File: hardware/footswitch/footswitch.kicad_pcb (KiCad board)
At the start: 2 copper layers, 34 x 58 mm, 6 parts, among them J1 Conn_02x05_Counter_Clockwise

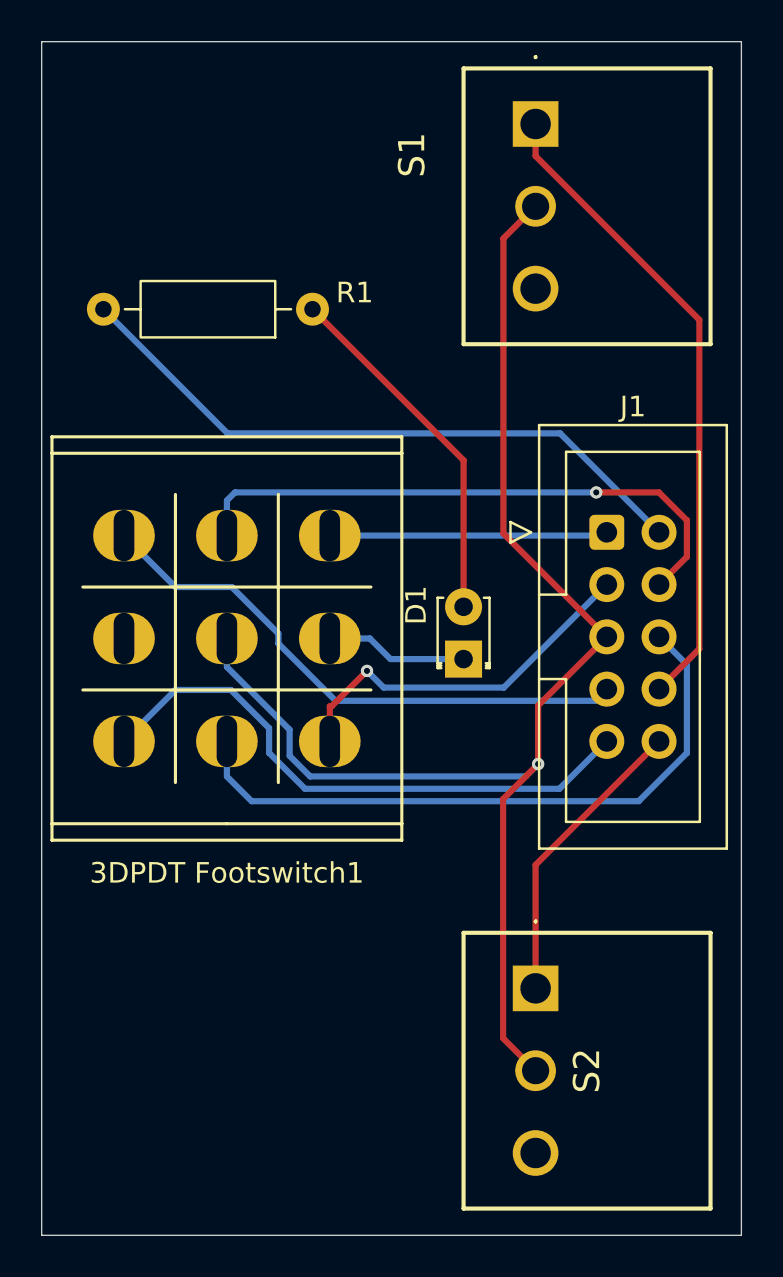
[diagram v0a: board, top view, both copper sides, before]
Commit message: Track adjustments to footswitch board
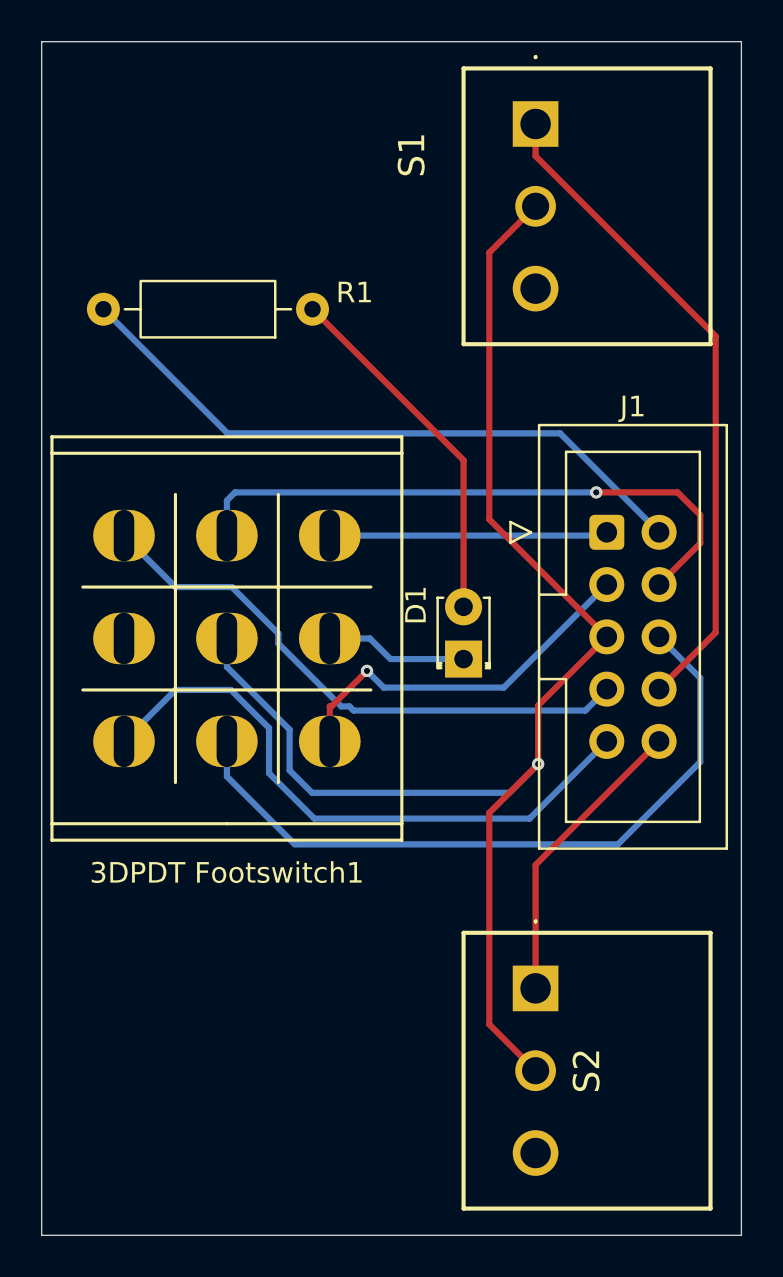
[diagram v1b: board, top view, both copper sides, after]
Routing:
- net /conn6: track 31.7 -> 34.6 mm
- net /conn5: track 67.2 -> 69.4 mm
- net /conn9: track 28.1 -> 29.9 mm
- net /conn4: track 28.5 -> 29.5 mm
- net /conn8: track 31.6 -> 32.2 mm
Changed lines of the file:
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@@
 	)
 	(segment
-		(start 157.46 99)
-		(end 155.1566 101.3034)
-		(width 0.3)
-		(layer "B.Cu")
-		(net 2)
-	)
-	(segment
-		(start 155.1566 101.3034)
-		(end 142.7959 101.3034)
+		(start 143.25 102.75)
+		(end 141.0511 100.5511)
+		(width 0.3)
+		(layer "B.Cu")
+		(net 2)
+	)
+	(segment
+		(start 141.0511 98.3552)
+		(end 139.1959 96.5)
+		(width 0.3)
+		(layer "B.Cu")
+		(net 2)
+	)
+	(segment
+		(start 136.5 96.5)
+		(end 134 99)
 		(width 0.3)
 		(layer "B.Cu")
@@
 	)
 	(segment
-		(start 142.7959 101.3034)
-		(end 141.0511 99.5586)
-		(width 0.3)
-		(layer "B.Cu")
-		(net 2)
-	)
-	(segment
-		(start 141.0511 99.5586)
+		(start 141.0511 100.5511)
 		(end 141.0511 98.3552)
 		(width 0.3)
@@
 	)
 	(segment
-		(start 141.0511 98.3552)
-		(end 139.1959 96.5)
-		(width 0.3)
-		(layer "B.Cu")
-		(net 2)
-	)
-	(segment
-		(start 136.5 96.5)
-		(end 134 99)
-		(width 0.3)
-		(layer "B.Cu")
-		(net 2)
+		(start 157.46 99)
+		(end 153.71 102.75)
+		(width 0.3)
+		(layer "B.Cu")
+		(net 2)
+	)
+	(segment
+		(start 153.71 102.75)
+		(end 143.25 102.75)
+		(width 0.3)
+		(layer "B.Cu")
+		(net 2)
+	)
+	(segment
+		(start 162 89.38)
+		(end 162 88)
+		(width 0.3)
+		(layer "F.Cu")
+		(net 3)
+	)
+	(segment
+		(start 160.9023 86.9023)
+		(end 156.9469 86.9023)
+		(width 0.3)
+		(layer "F.Cu")
+		(net 3)
+	)
+	(segment
+		(start 162 88)
+		(end 160.9023 86.9023)
+		(width 0.3)
+		(layer "F.Cu")
+		(net 3)
 	)
 	(segment
 		(start 160 91.38)
-		(end 161.3519 90.0281)
-		(width 0.3)
-		(layer "F.Cu")
-		(net 3)
-	)
-	(segment
-		(start 159.9971 86.9023)
-		(end 156.9469 86.9023)
-		(width 0.3)
-		(layer "F.Cu")
-		(net 3)
-	)
-	(segment
-		(start 161.3519 88.2571)
-		(end 159.9971 86.9023)
-		(width 0.3)
-		(layer "F.Cu")
-		(net 3)
-	)
-	(segment
-		(start 161.3519 90.0281)
-		(end 161.3519 88.2571)
+		(end 162 89.38)
 		(width 0.3)
 		(layer "F.Cu")
@@
 	)
 	(segment
+		(start 144.5542 97.299)
+		(end 141.5 94.2448)
+		(width 0.3)
+		(layer "B.Cu")
+		(net 5)
+	)
+	(segment
 		(start 141.5 94.2448)
 		(end 141.5 93.7597)
@@
 	)
 	(segment
-		(start 156.8917 97.0283)
-		(end 144.2835 97.0283)
+		(start 141.5 93.7597)
+		(end 139.2403 91.5)
+		(width 0.3)
+		(layer "B.Cu")
+		(net 5)
+	)
+	(segment
+		(start 145.155577 97.5)
+		(end 144.954577 97.299)
 		(width 0.3)
 		(layer "B.Cu")
@@
 	)
 	(segment
+		(start 156.42 97.5)
+		(end 145.155577 97.5)
+		(width 0.3)
+		(layer "B.Cu")
+		(net 5)
+	)
+	(segment
+		(start 144.954577 97.299)
+		(end 144.5542 97.299)
+		(width 0.3)
+		(layer "B.Cu")
+		(net 5)
+	)
+	(segment
 		(start 157.46 96.46)
-		(end 156.8917 97.0283)
+		(end 156.42 97.5)
 		(width 0.3)
 		(layer "B.Cu")
@@
 		(start 136.5 91.5)
 		(end 134 89)
-		(width 0.3)
-		(layer "B.Cu")
-		(net 5)
-	)
-	(segment
-		(start 141.5 93.7597)
-		(end 139.2403 91.5)
-		(width 0.3)
-		(layer "B.Cu")
-		(net 5)
-	)
-	(segment
-		(start 144.2835 97.0283)
-		(end 141.5 94.2448)
 		(width 0.3)
 		(layer "B.Cu")
@@
 	)
 	(segment
-		(start 159.0079 101.9051)
-		(end 161.3508 99.5622)
-		(width 0.3)
-		(layer "B.Cu")
-		(net 7)
-	)
-	(segment
 		(start 139 99)
 		(end 139 100.7017)
@@
 	)
 	(segment
-		(start 161.3508 99.5622)
-		(end 161.3508 95.2708)
-		(width 0.3)
-		(layer "B.Cu")
-		(net 7)
-	)
-	(segment
-		(start 161.3508 95.2708)
+		(start 142.2983 104)
+		(end 158 104)
+		(width 0.3)
+		(layer "B.Cu")
+		(net 7)
+	)
+	(segment
+		(start 139 100.7017)
+		(end 142.2983 104)
+		(width 0.3)
+		(layer "B.Cu")
+		(net 7)
+	)
+	(segment
+		(start 162 95.92)
 		(end 160 93.92)
 		(width 0.3)
@@
 	)
 	(segment
-		(start 139 100.7017)
-		(end 140.2034 101.9051)
-		(width 0.3)
-		(layer "B.Cu")
-		(net 7)
-	)
-	(segment
-		(start 140.2034 101.9051)
-		(end 159.0079 101.9051)
+		(start 158 104)
+		(end 162 100)
+		(width 0.3)
+		(layer "B.Cu")
+		(net 7)
+	)
+	(segment
+		(start 162 100)
+		(end 162 95.92)
 		(width 0.3)
 		(layer "B.Cu")
@@
 	)
 	(segment
-		(start 154 73)
-		(end 152.438 74.562)
-		(width 0.3)
-		(layer "F.Cu")
-		(net 9)
-	)
-	(segment
-		(start 152.4226 113.4226)
-		(end 152.4226 101.8022)
-		(width 0.3)
-		(layer "F.Cu")
-		(net 9)
-	)
-	(segment
 		(start 154.125 97.255)
 		(end 157.46 93.92)
@@
 	)
 	(segment
-		(start 152.438 74.562)
-		(end 152.438 88.898)
-		(width 0.3)
-		(layer "F.Cu")
-		(net 9)
-	)
-	(segment
-		(start 152.438 88.898)
+		(start 151.75 88.21)
 		(end 157.46 93.92)
 		(width 0.3)
@@
 	)
 	(segment
-		(start 152.4226 101.8022)
-		(end 154.125 100.0998)
+		(start 154 115)
+		(end 151.75 112.75)
+		(width 0.3)
+		(layer "F.Cu")
+		(net 9)
+	)
+	(segment
+		(start 151.75 75.25)
+		(end 151.75 88.21)
 		(width 0.3)
 		(layer "F.Cu")
@@
 	)
 	(segment
-		(start 154 115)
-		(end 152.4226 113.4226)
+		(start 151.75 112.75)
+		(end 151.75 102.4748)
+		(width 0.3)
+		(layer "F.Cu")
+		(net 9)
+	)
+	(segment
+		(start 154 73)
+		(end 151.75 75.25)
+		(width 0.3)
+		(layer "F.Cu")
+		(net 9)
+	)
+	(segment
+		(start 151.75 102.4748)
+		(end 154.125 100.0998)
 		(width 0.3)
 		(layer "F.Cu")
@@
 	)
 	(segment
-		(start 143.0451 100.7017)
-		(end 153.5231 100.7017)
-		(width 0.3)
-		(layer "B.Cu")
-		(net 9)
-	)
-	(segment
 		(start 142.0483 98.4309)
-		(end 142.0483 99.7049)
+		(end 142.0483 100.40609)
+		(width 0.3)
+		(layer "B.Cu")
+		(net 9)
+	)
+	(segment
+		(start 142.0483 100.40609)
+		(end 143.14221 101.5)
+		(width 0.3)
+		(layer "B.Cu")
+		(net 9)
+	)
+	(segment
+		(start 143.14221 101.5)
+		(end 152.7248 101.5)
+		(width 0.3)
+		(layer "B.Cu")
+		(net 9)
+	)
+	(segment
+		(start 152.7248 101.5)
+		(end 154.125 100.0998)
 		(width 0.3)
 		(layer "B.Cu")
@@
 	)
 	(segment
-		(start 153.5231 100.7017)
-		(end 154.125 100.0998)
-		(width 0.3)
-		(layer "B.Cu")
-		(net 9)
-	)
-	(segment
 		(start 139 95.3826)
 		(end 142.0483 98.4309)
@@
 	)
 	(segment
-		(start 142.0483 99.7049)
-		(end 143.0451 100.7017)
-		(width 0.3)
-		(layer "B.Cu")
-		(net 9)
+		(start 162.75 93.71)
+		(end 162.75 79.3117)
+		(width 0.3)
+		(layer "F.Cu")
+		(net 10)
+	)
+	(segment
+		(start 162.75 79.3117)
+		(end 154 70.5617)
+		(width 0.3)
+		(layer "F.Cu")
+		(net 10)
+	)
+	(segment
+		(start 154 70.5617)
+		(end 154 69)
+		(width 0.3)
+		(layer "F.Cu")
+		(net 10)
 	)
 	(segment
 		(start 160 96.46)
-		(end 161.9536 94.5064)
-		(width 0.3)
-		(layer "F.Cu")
-		(net 10)
-	)
-	(segment
-		(start 154 69)
-		(end 154 70.5617)
-		(width 0.3)
-		(layer "F.Cu")
-		(net 10)
-	)
-	(segment
-		(start 161.9536 94.5064)
-		(end 161.9536 78.5153)
-		(width 0.3)
-		(layer "F.Cu")
-		(net 10)
-	)
-	(segment
-		(start 161.9536 78.5153)
-		(end 154 70.5617)
-		(width 0.3)
-		(layer "F.Cu")
+		(end 162.75 93.71)
+		(width 0.3)
+		(layer "F.Cu")

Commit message: Adjust footprint for dpdt alpha
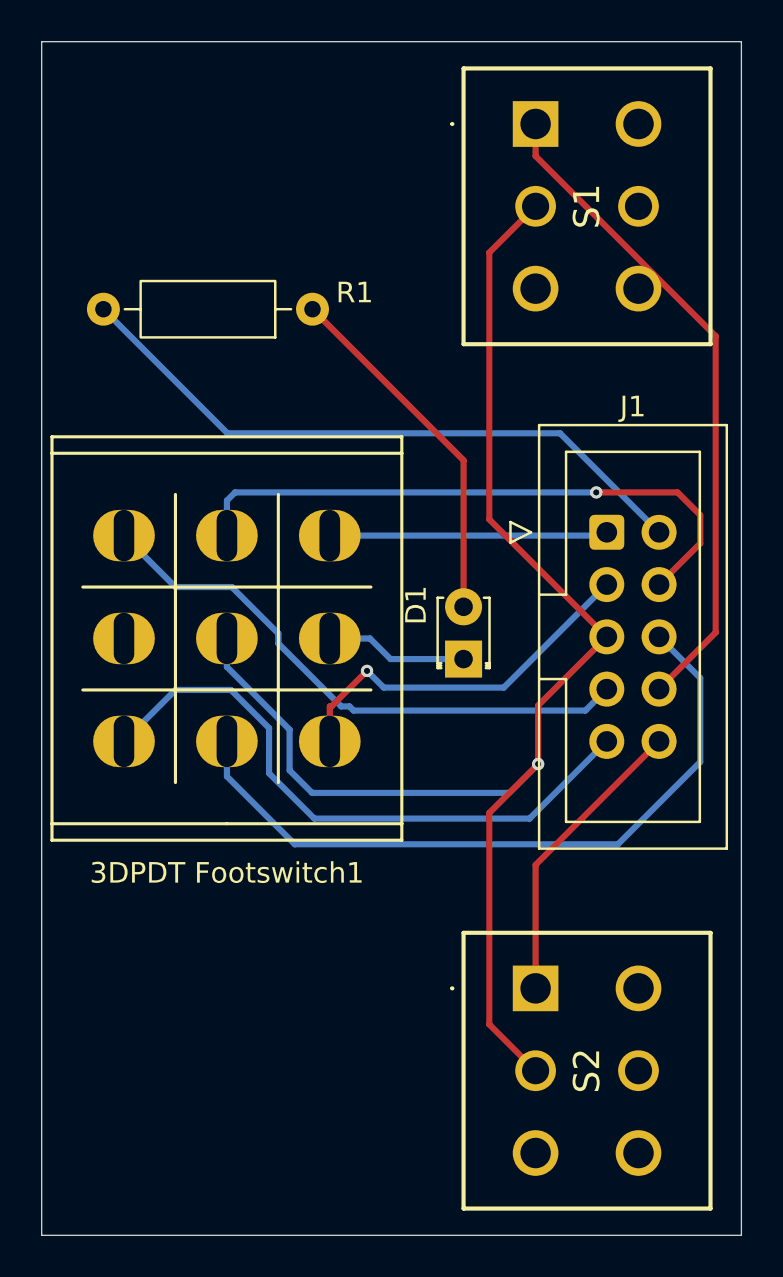
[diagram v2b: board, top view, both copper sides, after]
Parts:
- S1, S2: footprint pcb switch:SF12011F010220RM050 -> pcb switch:DPDT momentary footswitch

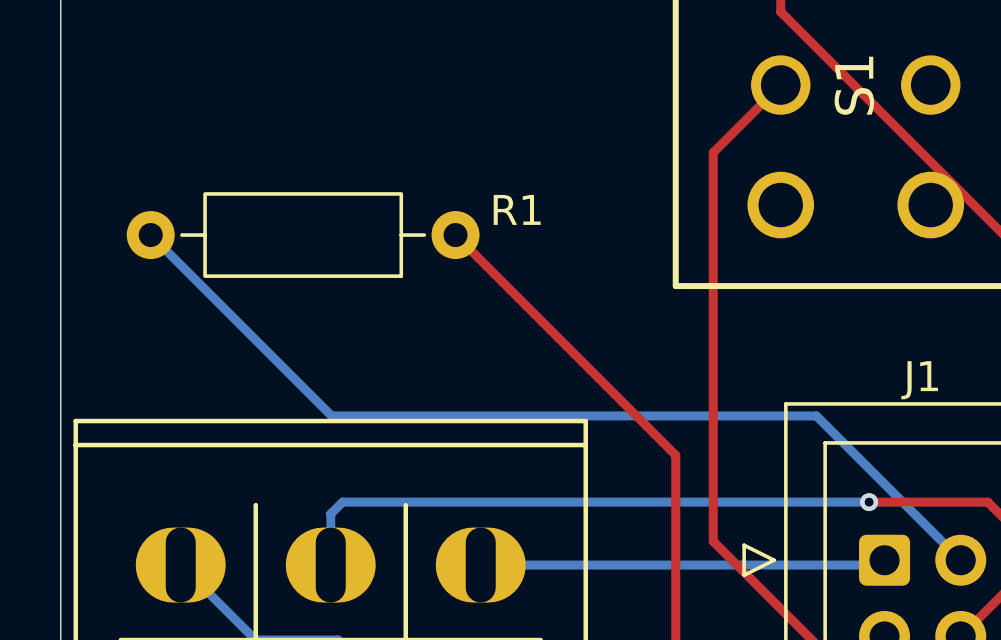
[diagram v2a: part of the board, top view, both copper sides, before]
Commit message: Move resistor so switch sections could be cut off
Might want a different switch connected directly to main pcb
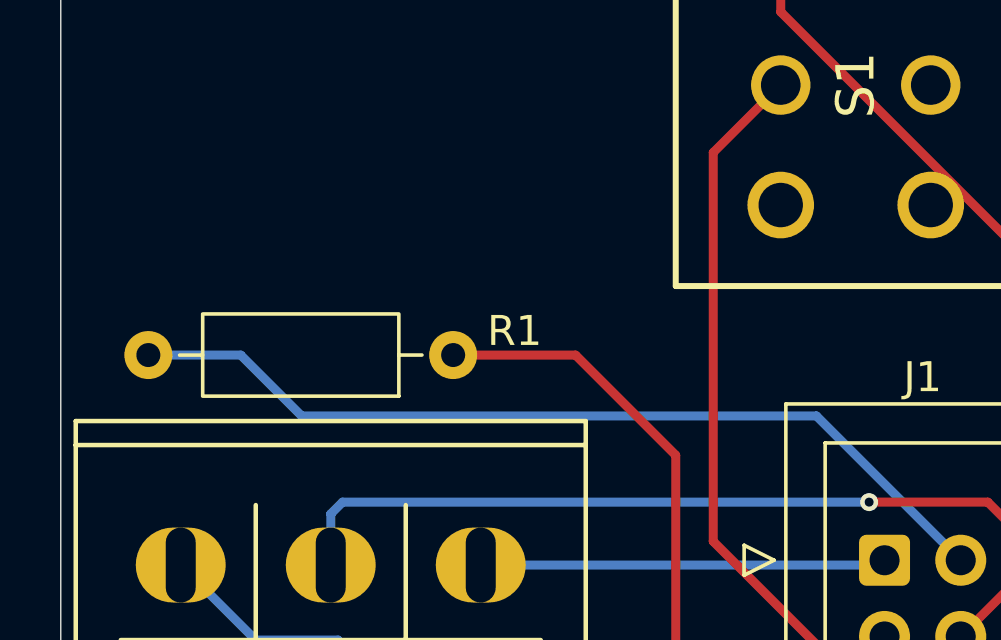
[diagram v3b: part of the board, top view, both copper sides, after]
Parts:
- moved R1 4.00 mm to (143.1, 82.0)
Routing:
- net Net-(D1-A): track 17.5 -> 15.9 mm
- net /conn2: track 31.5 -> 29.9 mm
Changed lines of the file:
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@@
 	(footprint "Resistor_THT:R_Axial_DIN0207_L6.3mm_D2.5mm_P10.16mm_Horizontal"
 		(layer "F.Cu")
-		(at 143.16 78 180)
+		(at 143.08 82 180)
 		(descr "Resistor, Axial_DIN0207 series, Axial, Horizontal, pin pitch=10.16mm, 0.25W = 1/4W, length*diameter=6.3*2.5mm^2, http://cdn-reichelt.de/documents/datenblatt/B400/1_4W%23YAG.pdf")
 		(tags "Resistor Axial_DIN0207 series Axial Horizontal pin pitch 10.16mm 0.25W = 1/4W length 6.3mm diameter 2.5mm")
@@
 	)
 	(segment
+		(start 155.1899 84.0299)
+		(end 138.0299 84.0299)
+		(width 0.3)
+		(layer "B.Cu")
+		(net 4)
+	)
+	(segment
 		(start 160 88.84)
 		(end 155.1899 84.0299)
@@
 	)
 	(segment
-		(start 139.0299 84.0299)
-		(end 133 78)
+		(start 136 82)
+		(end 132.92 82)
 		(width 0.3)
 		(layer "B.Cu")
@@
 	)
 	(segment
-		(start 155.1899 84.0299)
-		(end 139.0299 84.0299)
+		(start 138.0299 84.0299)
+		(end 136 82)
 		(width 0.3)
 		(layer "B.Cu")
@@
 	(segment
 		(start 150.5 85.34)
+		(end 147.16 82)
+		(width 0.3)
+		(layer "F.Cu")
+		(net 11)
+	)
+	(segment
+		(start 150.5 85.34)
 		(end 150.5 92.46)
 		(width 0.3)
@@
 	)
 	(segment
-		(start 143.16 78)
-		(end 150.5 85.34)
-		(width 0.3)
-		(layer "F.Cu")
+		(start 147.16 82)
+		(end 143.08 82)
+		(width 0.3)
+		(layer "F.Cu")
